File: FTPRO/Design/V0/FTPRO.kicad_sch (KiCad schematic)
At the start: 5 parts

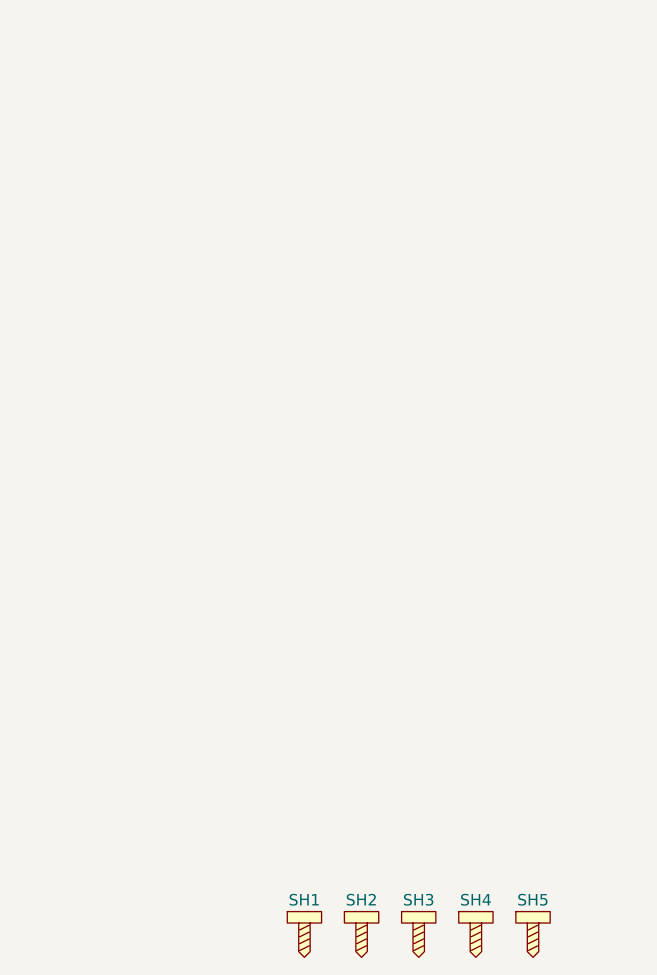
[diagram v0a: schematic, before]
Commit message: PCB Outline
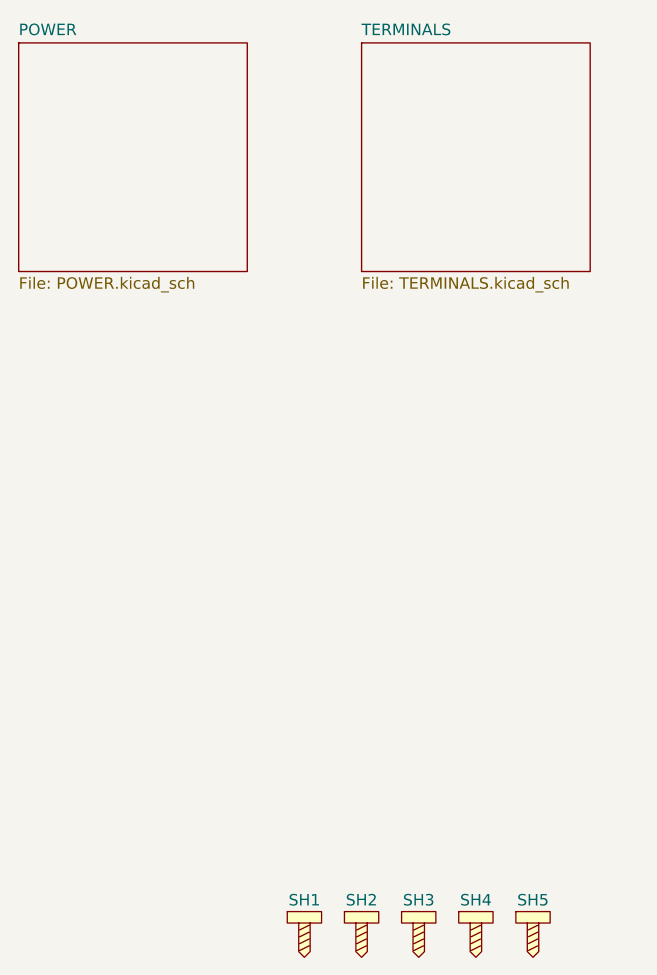
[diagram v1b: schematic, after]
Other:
- added sheet POWER (POWER.kicad_sch)
- added sheet TERMINALS (TERMINALS.kicad_sch)
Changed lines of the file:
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@@
+		)
+	)
+	(sheet
+		(at 31.75 25.4)
+		(size 25.4 25.4)
+		(fields_autoplaced yes)
+		(stroke
+			(width 0.1524)
+			(type solid)
+		)
+		(fill
+			(color 0 0 0 0.0000)
+		)
+		(property "Sheetname" "POWER"
+			(at 31.75 24.6884 0)
+			(effects
+				(font
+					(size 1.27 1.27)
+				)
+				(justify left bottom)
+			)
+		)
+		(property "Sheetfile" "POWER.kicad_sch"
+			(at 31.75 51.3846 0)
+			(effects
+				(font
+					(size 1.27 1.27)
+				)
+				(justify left top)
+			)
+		)
+		(instances
+			(project "FTPRO"
+				(path "/23049313-8394-4ad2-b0e9-99c19e3c74e9"
+					(page "2")
+				)
+			)
+		)
+	)
+	(sheet
+		(at 69.85 25.4)
+		(size 25.4 25.4)
+		(fields_autoplaced yes)
+		(stroke
+			(width 0.1524)
+			(type solid)
+		)
+		(fill
+			(color 0 0 0 0.0000)
+		)
+		(property "Sheetname" "TERMINALS"
+			(at 69.85 24.6884 0)
+			(effects
+				(font
+					(size 1.27 1.27)
+				)
+				(justify left bottom)
+			)
+		)
+		(property "Sheetfile" "TERMINALS.kicad_sch"
+			(at 69.85 51.3846 0)
+			(effects
+				(font
+					(size 1.27 1.27)
+				)
+				(justify left top)
+			)
+		)
+		(instances
+			(project "FTPRO"
+				(path "/23049313-8394-4ad2-b0e9-99c19e3c74e9"
+					(page "3")
+				)
+			)
 		)
 	)
